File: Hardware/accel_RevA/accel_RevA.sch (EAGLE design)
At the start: 13 parts, among them U1 MMA8452Q

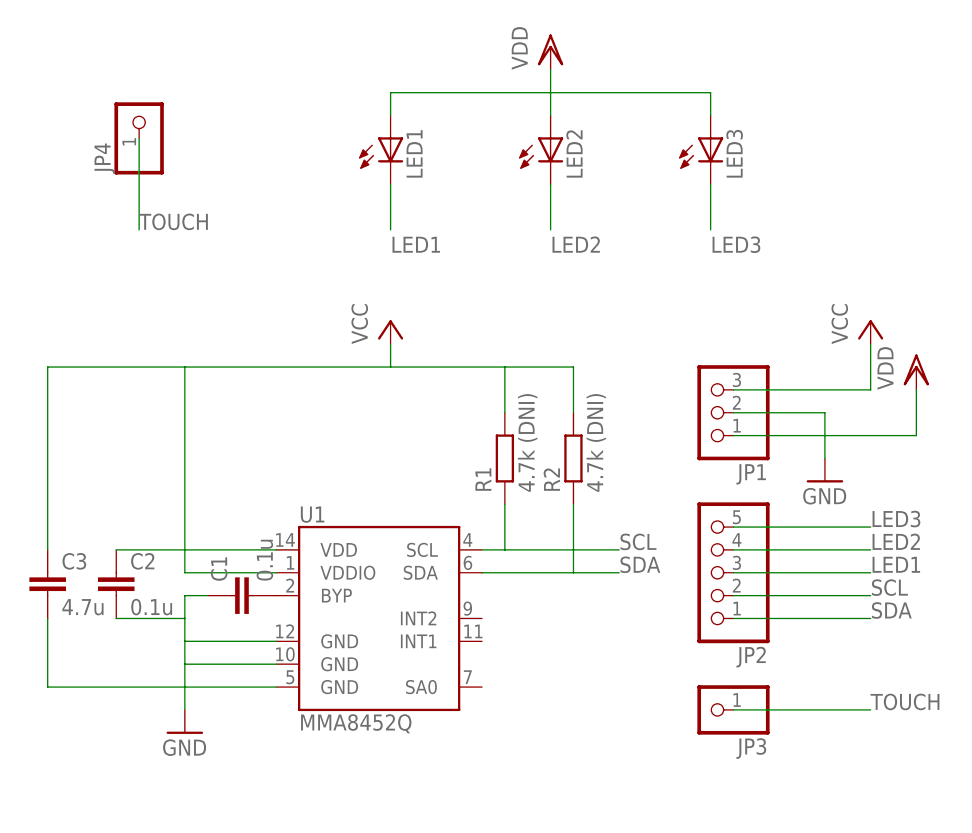
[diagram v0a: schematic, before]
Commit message: Update of accel board and schem
Moved about stuff, added silkscreen cut guide, removed pullups on I2C (
will be included on microcontroller )
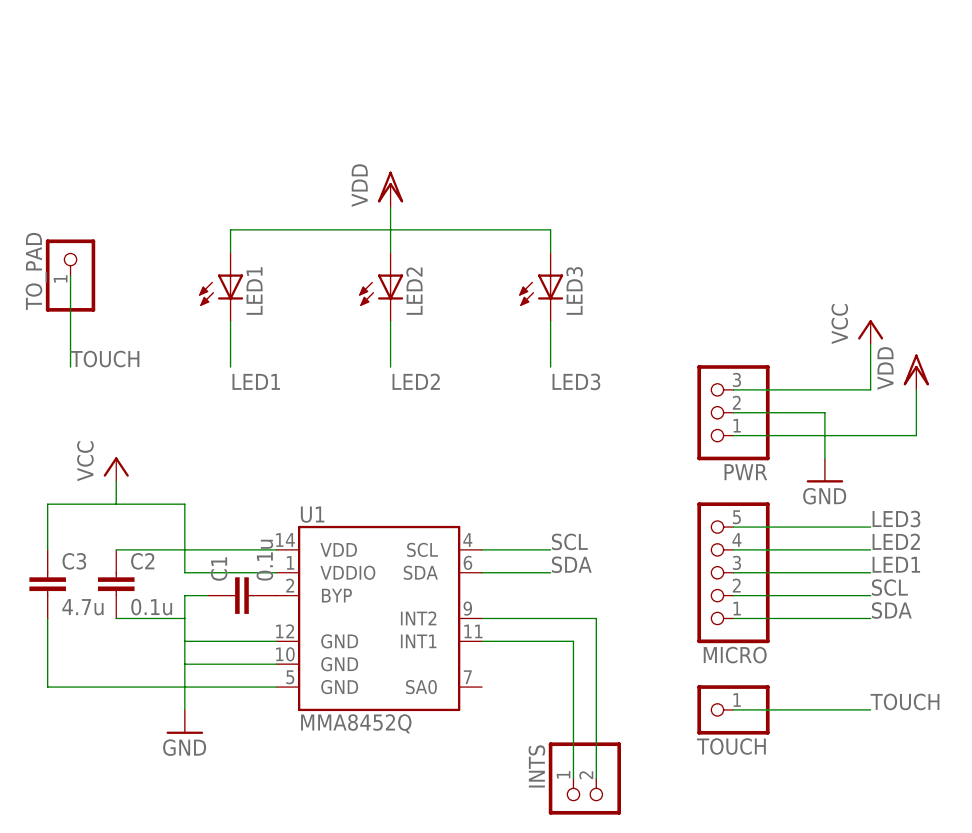
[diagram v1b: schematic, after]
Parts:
- removed JP4: (no value), pinhead:PINHD-1X1
- removed R1, R2: 4.7k (DNI), eagle-ltspice:RR0603
- added INTS: (no value), pinhead:PINHD-1X2
- added TO_PAD: (no value), pinhead:PINHD-1X1
- renumbered JP1 to PWR, JP2 to MICRO, JP3 to TOUCH
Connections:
- new net N$1: INTS.1, U1.INT1
- new net N$2: INTS.2, U1.INT2
- net SCL: no longer R1.1
- net SDA: no longer R2.1
- net TOUCH: now also TO_PAD.1; no longer JP4.1
- net VCC: no longer R1.2, R2.2
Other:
- moved on the sheet: LED1, LED2, LED3

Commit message: Update of revA of accel board
Completed routing of board!! No rats nest left, passes DRC and ERC.
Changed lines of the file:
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@@
 <wire x1="7.62" y1="48.26" x2="7.62" y2="40.64" width="0.1524" layer="91"/>
 <wire x1="7.62" y1="40.64" x2="22.86" y2="40.64" width="0.1524" layer="91"/>
+<junction x="22.86" y="48.26"/>
+<junction x="22.86" y="45.72"/>
+<junction x="22.86" y="43.18"/>
+<junction x="22.86" y="40.64"/>
 </segment>
 <segment>
@@
 <pinref part="P+1" gate="VCC" pin="VCC"/>
 <wire x1="15.24" y1="63.5" x2="15.24" y2="60.96" width="0.1524" layer="91"/>
+<junction x="22.86" y="55.88"/>
+<junction x="15.24" y="60.96"/>
 </segment>
 </net>
@@
 <wire x1="45.72" y1="91.44" x2="45.72" y2="93.98" width="0.1524" layer="91"/>
 <pinref part="VDD2" gate="G$1" pin="VDD"/>
+<junction x="45.72" y="91.44"/>
 </segment>
 </net>
